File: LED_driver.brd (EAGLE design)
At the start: 53.3 x 25.4 mm, 16 parts

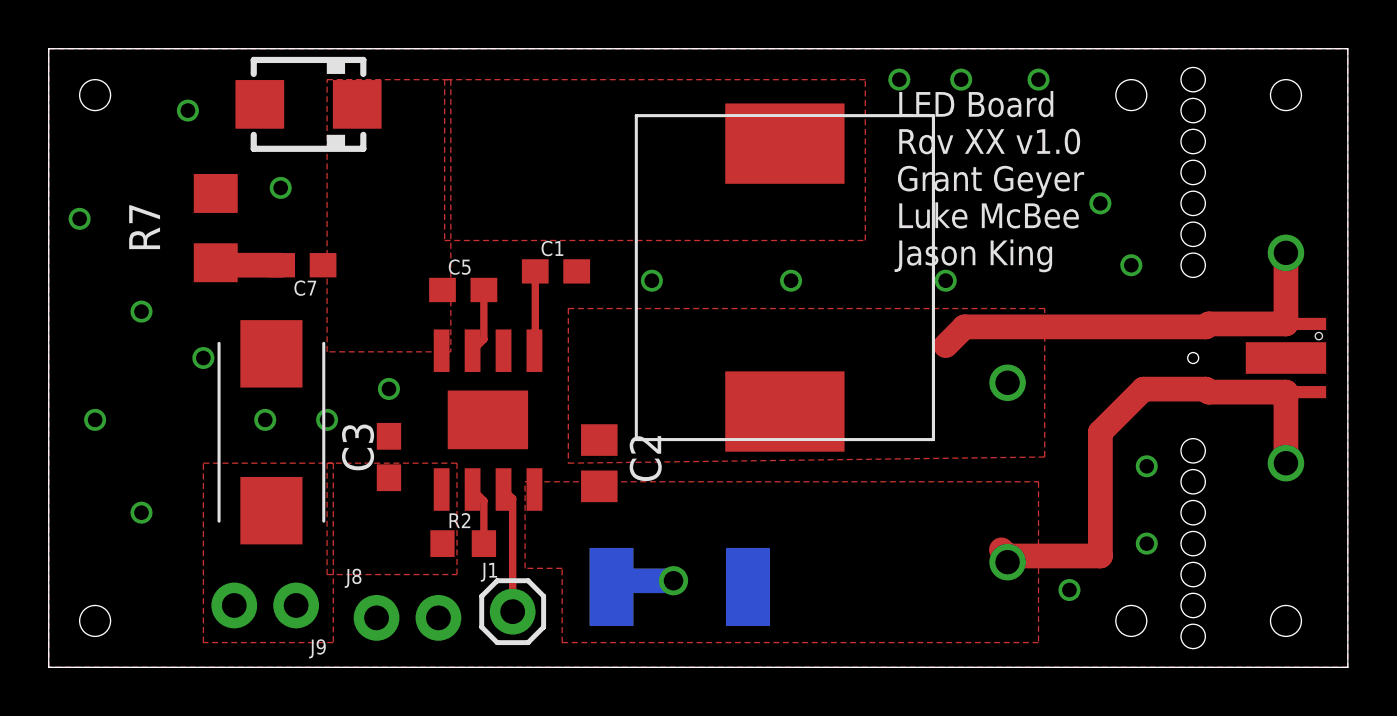
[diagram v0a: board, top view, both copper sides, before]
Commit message: added nmos and connected EN to 12V
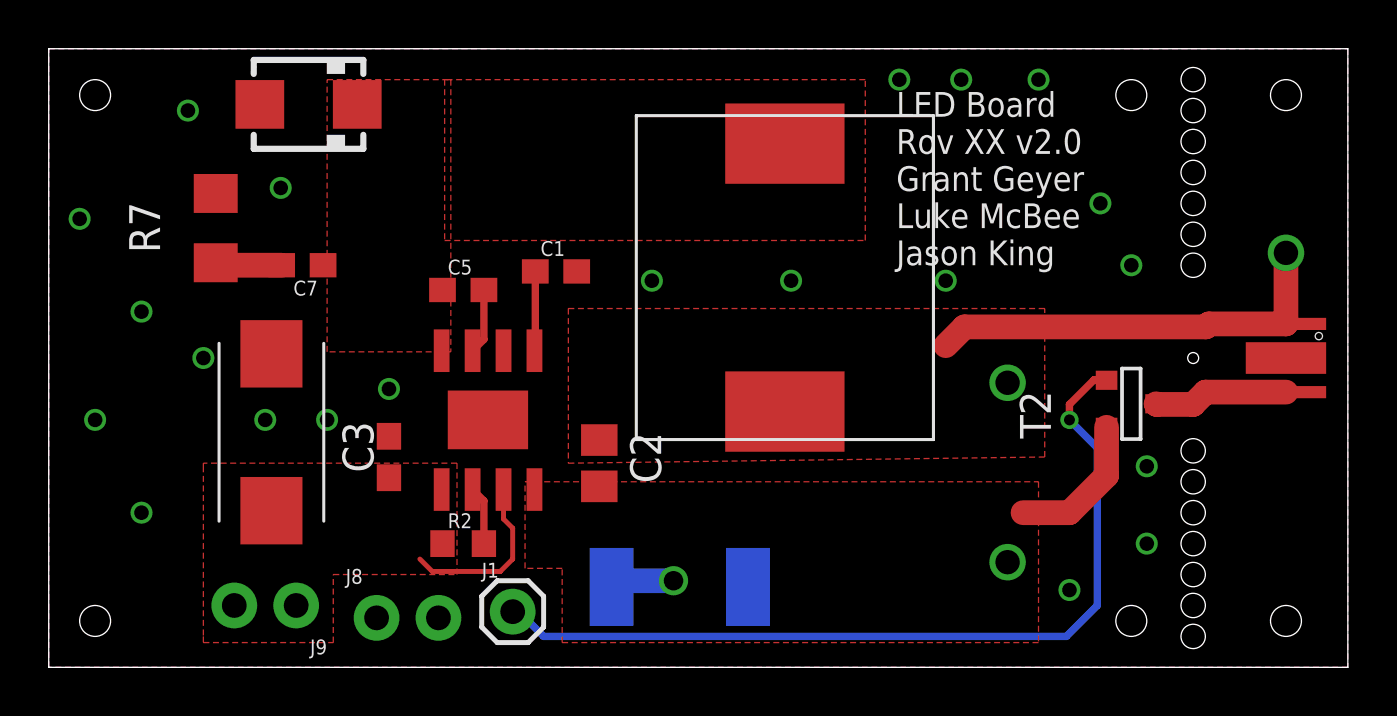
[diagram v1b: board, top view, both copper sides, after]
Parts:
- added T2: (no value), zetex:SOT-23
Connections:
- removed net LED-PWM: J1.1, U$1.3
- removed net VIN: C3.1, C8.+, J9.1, J9.2, R2.1, U$1.1
- new net 12V: C3.1, C8.+, J9.1, J9.2, R2.1, U$1.1, U$1.3
- new net LED_PWM: J1.1, T2.3
- new net N$3: T2.1, U$3.LED-
- net LED-: now also T2.2; no longer U$3.LED-
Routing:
- net LED_PWM: track 0.00 -> 35.6 mm, vias 0 -> 1
- net LED-: track 23.2 -> 8.69 mm, vias 3 -> 2
- net 12V: track 0.00 -> 7.24 mm
- net N$3: track 0.00 -> 5.55 mm
- net LED-PWM: track 5.17 -> 0.00 mm
- added copper zone on layer 1, net 12V
- removed copper zone on layer 1, net VIN
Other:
- board text added: "LED Board Rov XX v2.0 Grant Geyer Luke McBee Jason King"
- board text removed: "LED Board Rov XX v1.0 Grant Geyer Luke McBee Jason King"
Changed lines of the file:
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@@
 <?xml version="1.0" encoding="utf-8"?>
 <!DOCTYPE eagle SYSTEM "eagle.dtd">
-<eagle version="8.4.1">
+<eagle version="8.3.2">
 <drawing>
 <settings>
@@
 <setting verticaltext="up"/>
 </settings>
-<grid distance="25" unitdist="mil" unit="mil" style="lines" multiple="1" display="no" altdistance="5" altunitdist="mil" altunit="mil"/>
+<grid distance="10" unitdist="mil" unit="mil" style="lines" multiple="1" display="no" altdistance="5" altunitdist="mil" altunit="mil"/>
 <layers>
 <layer number="1" name="Top" color="4" fill="1" visible="yes" active="yes"/>
@@
 <wire x1="-5.08" y1="25.4" x2="-5.08" y2="0" width="0" layer="20"/>
 <text x="29.718" y="16.51" size="1.016" layer="21">LED Board
-Rov XX v1.0
+Rov XX v2.0
 Grant Geyer
 Luke McBee
@@
 <param name="dpMaxLengthDifference" value="10mm"/>
 <param name="dpGapFactor" value="2.5"/>
+<param name="checkGrid" value="0"/>
 <param name="checkAngle" value="0"/>
 <param name="checkFont" value="1"/>
 <param name="checkRestrict" value="0"/>
-<param name="checkStop" value="0"/>
 <param name="useDiameter" value="13"/>
 <param name="maxErrors" value="50"/>
@@
 <element name="J9" library="SparkFun-Connectors" library_urn="urn:adsk.eagle:library:513" package="1X02_NO_SILK" package3d_urn="urn:adsk.eagle:package:38051/1" value="" x="5.08" y="2.54" rot="R180"/>
 <element name="U$3" library="LED_00H53" package="LED_00H53" value="LED_00H53" x="45.72" y="12.7" rot="R270"/>
+<element name="T2" library="zetex" package="SOT-23" value="" x="39.37" y="10.795" rot="R90">
+<attribute name="MF" value="" x="31.115" y="2.54" size="1.778" layer="27" rot="R90" display="off"/>
+<attribute name="MPN" value="" x="31.115" y="2.54" size="1.778" layer="27" rot="R90" display="off"/>
+<attribute name="OC_FARNELL" value="unknown" x="31.115" y="2.54" size="1.778" layer="27" rot="R90" display="off"/>
+<attribute name="OC_NEWARK" value="unknown" x="31.115" y="2.54" size="1.778" layer="27" rot="R90" display="off"/>
+</element>
 </elements>
 <signals>
@@
 <wire x1="12.788" y1="6.836" x2="12.324" y2="7.3" width="0.3048" layer="1"/>
 </signal>
-<signal name="VIN">
+<signal name="12V">
+<contactref element="U$1" pad="3"/>
 <contactref element="U$1" pad="1"/>
 <contactref element="R2" pad="1"/>
 <contactref element="C8" pad="+"/>
 <contactref element="C3" pad="1"/>
+<wire x1="13.594" y1="7.3" x2="13.594" y2="6.091" width="0.2032" layer="1"/>
+<wire x1="13.594" y1="6.091" x2="13.97" y2="5.715" width="0.2032" layer="1"/>
+<wire x1="13.97" y1="5.715" x2="13.97" y2="4.445" width="0.2032" layer="1"/>
+<wire x1="13.97" y1="4.445" x2="13.462" y2="3.937" width="0.2032" layer="1"/>
+<wire x1="10.668" y1="3.937" x2="10.16" y2="4.445" width="0.2032" layer="1"/>
+<wire x1="13.462" y1="3.937" x2="10.668" y2="3.937" width="0.2032" layer="1"/>
 <contactref element="J9" pad="2"/>
 <contactref element="J9" pad="1"/>
-<polygon width="0.1524" layer="1">
+<polygon width="0.2032" layer="1">
+<vertex x="1.27" y="8.255"/>
+<vertex x="1.27" y="1.27"/>
 <vertex x="1.27" y="1.016"/>
-<vertex x="1.27" y="8.382"/>
-<vertex x="6.604" y="8.382"/>
 <vertex x="6.604" y="1.016"/>
-</polygon>
-<polygon width="0.1524" layer="1">
-<vertex x="6.35" y="3.81"/>
+<vertex x="6.604" y="3.81"/>
 <vertex x="11.684" y="3.81"/>
 <vertex x="11.684" y="8.382"/>
-<vertex x="6.35" y="8.382"/>
-</polygon>
-</signal>
-<signal name="LED-PWM">
-<contactref element="U$1" pad="3"/>
-<contactref element="J1" pad="1"/>
-<wire x1="13.97" y1="2.286" x2="13.97" y2="6.924" width="0.3048" layer="1"/>
-<wire x1="13.97" y1="6.924" x2="13.594" y2="7.3" width="0.3048" layer="1"/>
+<vertex x="1.27" y="8.382"/>
+</polygon>
 </signal>
 <signal name="N$4">
@@
 <contactref element="R1" pad="2"/>
 <contactref element="U$1" pad="4"/>
-<contactref element="U$3" pad="LED-"/>
 <polygon width="0.3048" layer="1">
 <vertex x="14.478" y="7.62"/>
@@
 <wire x1="20.574" y1="3.556" x2="18.282" y2="3.556" width="1.016" layer="16"/>
 <wire x1="18.282" y1="3.556" x2="18.028" y2="3.302" width="1.016" layer="16"/>
-<wire x1="42.55474375" y1="11.3" x2="45.72" y2="11.3" width="1.016" layer="1"/>
-<wire x1="42.55474375" y1="11.3" x2="42.43274375" y2="11.422" width="1.016" layer="1"/>
-<wire x1="42.43274375" y1="11.422" x2="39.87" y2="11.422" width="1.016" layer="1"/>
-<wire x1="38.1" y1="9.652" x2="38.1" y2="4.572" width="1.016" layer="1"/>
-<wire x1="38.1" y1="4.572" x2="34.29" y2="4.572" width="1.016" layer="1"/>
-<wire x1="34.29" y1="4.572" x2="34.036" y2="4.826" width="1.016" layer="1"/>
-<wire x1="39.87" y1="11.422" x2="38.1" y2="9.652" width="1.016" layer="1"/>
 <via x="34.29" y="4.318" extent="1-16" drill="1"/>
-<via x="45.72" y="8.382" extent="1-16" drill="1"/>
-<wire x1="45.72" y1="11.3" x2="45.72" y2="8.382" width="1.016" layer="1"/>
+<contactref element="T2" pad="2"/>
+<wire x1="38.354" y1="9.8552" x2="38.354" y2="7.874" width="1.016" layer="1"/>
+<wire x1="38.354" y1="7.874" x2="36.83" y2="6.35" width="1.016" layer="1"/>
+<wire x1="36.83" y1="6.35" x2="34.925" y2="6.35" width="1.016" layer="1"/>
 </signal>
 <signal name="VCC6211">
@@
 <wire x1="1.88" y1="16.51" x2="1.778" y2="16.612" width="1.016" layer="1"/>
 </signal>
+<signal name="LED_PWM">
+<contactref element="J1" pad="1"/>
+<contactref element="T2" pad="3"/>
+<wire x1="13.97" y1="2.286" x2="14.224" y2="2.286" width="0.3048" layer="16"/>
+<wire x1="14.224" y1="2.286" x2="15.24" y2="1.27" width="0.3048" layer="16"/>
+<wire x1="15.24" y1="1.27" x2="36.703" y2="1.27" width="0.3048" layer="16"/>
+<wire x1="36.703" y1="1.27" x2="37.973" y2="2.54" width="0.3048" layer="16"/>
+<wire x1="37.973" y1="9.017" x2="37.973" y2="2.54" width="0.3048" layer="16"/>
+<wire x1="37.846" y1="11.811" x2="38.3286" y2="11.811" width="0.3048" layer="1"/>
+<wire x1="38.3286" y1="11.811" x2="38.354" y2="11.7856" width="0.3048" layer="1"/>
+<wire x1="37.846" y1="11.811" x2="36.83" y2="10.795" width="0.3048" layer="1"/>
+<wire x1="36.83" y1="10.795" x2="36.83" y2="10.16" width="0.3048" layer="1"/>
+<via x="36.83" y="10.16" extent="1-16" drill="0.45"/>
+<wire x1="36.83" y1="10.16" x2="37.973" y2="9.017" width="0.3048" layer="16"/>
+</signal>
+<signal name="N$3">
+<contactref element="T2" pad="1"/>
+<contactref element="U$3" pad="LED-"/>
+<wire x1="45.72" y1="11.3" x2="42.415" y2="11.3" width="1.016" layer="1"/>
+<wire x1="42.415" y1="11.3" x2="41.91" y2="10.795" width="1.016" layer="1"/>
+<wire x1="41.91" y1="10.795" x2="40.4114" y2="10.795" width="1.016" layer="1"/>
+<wire x1="40.4114" y1="10.795" x2="40.386" y2="10.8204" width="1.016" layer="1"/>
+</signal>
 </signals>

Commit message: moved mosfet so end can still be broken off
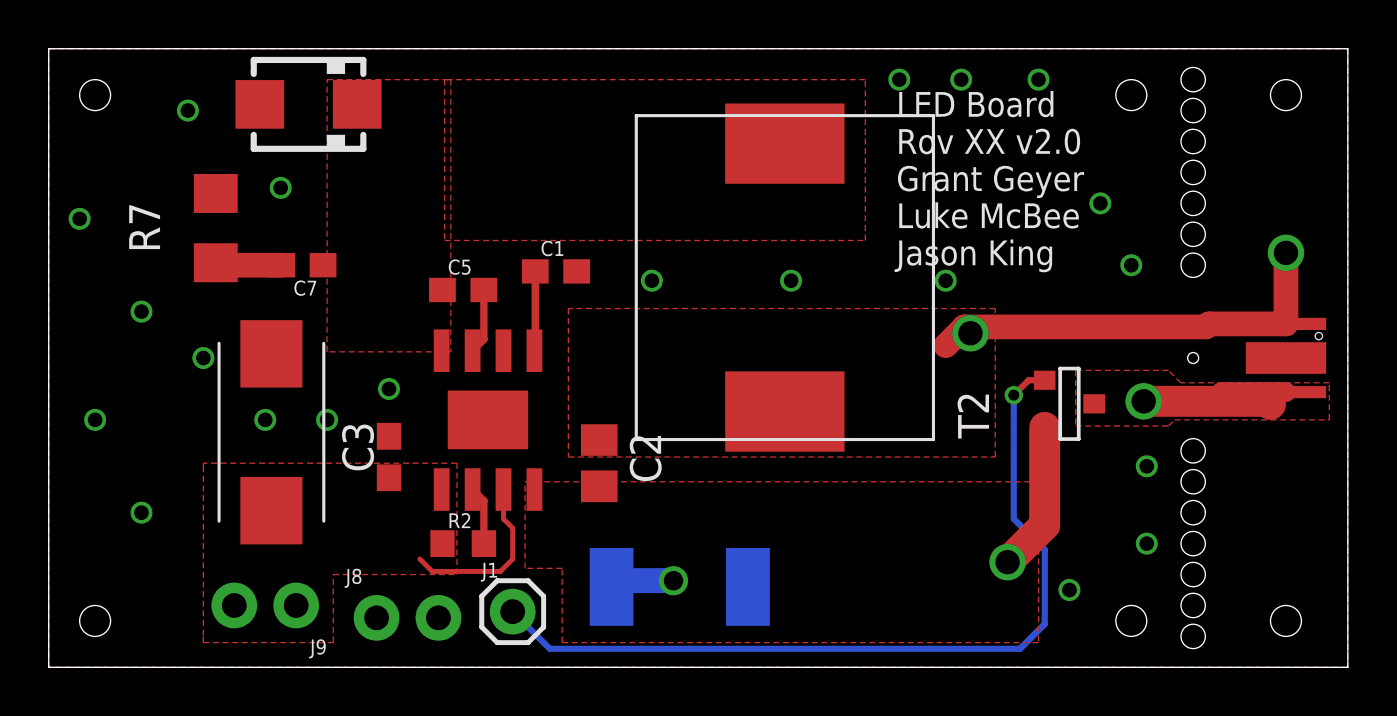
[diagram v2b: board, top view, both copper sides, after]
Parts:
- moved T2 2.54 mm to (36.8, 10.8)
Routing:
- net N$3: track 5.55 -> 7.92 mm, vias 0 -> 1
- net LED_PWM: track 35.6 -> 34.3 mm
- added copper zone on layer 1, net N$3
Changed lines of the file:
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@@
 <element name="J9" library="SparkFun-Connectors" library_urn="urn:adsk.eagle:library:513" package="1X02_NO_SILK" package3d_urn="urn:adsk.eagle:package:38051/1" value="" x="5.08" y="2.54" rot="R180"/>
 <element name="U$3" library="LED_00H53" package="LED_00H53" value="LED_00H53" x="45.72" y="12.7" rot="R270"/>
-<element name="T2" library="zetex" package="SOT-23" value="" x="39.37" y="10.795" rot="R90">
-<attribute name="MF" value="" x="31.115" y="2.54" size="1.778" layer="27" rot="R90" display="off"/>
-<attribute name="MPN" value="" x="31.115" y="2.54" size="1.778" layer="27" rot="R90" display="off"/>
-<attribute name="OC_FARNELL" value="unknown" x="31.115" y="2.54" size="1.778" layer="27" rot="R90" display="off"/>
-<attribute name="OC_NEWARK" value="unknown" x="31.115" y="2.54" size="1.778" layer="27" rot="R90" display="off"/>
+<element name="T2" library="zetex" package="SOT-23" value="" x="36.83" y="10.795" rot="R90">
+<attribute name="MF" value="" x="28.575" y="2.54" size="1.778" layer="27" rot="R90" display="off"/>
+<attribute name="MPN" value="" x="28.575" y="2.54" size="1.778" layer="27" rot="R90" display="off"/>
+<attribute name="OC_FARNELL" value="unknown" x="28.575" y="2.54" size="1.778" layer="27" rot="R90" display="off"/>
+<attribute name="OC_NEWARK" value="unknown" x="28.575" y="2.54" size="1.778" layer="27" rot="R90" display="off"/>
 </element>
 </elements>
@@
 <contactref element="U$4" pad="P$2"/>
 <contactref element="U$3" pad="LED+"/>
-<polygon width="0.3048" layer="1">
-<vertex x="16.256" y="8.382"/>
-<vertex x="35.814" y="8.636"/>
-<vertex x="35.814" y="14.732"/>
-<vertex x="16.256" y="14.732"/>
-</polygon>
 <wire x1="42.55474375" y1="14.1" x2="45.72" y2="14.1" width="1.016" layer="1"/>
 <wire x1="42.55474375" y1="14.1" x2="42.43274375" y2="13.978" width="1.016" layer="1"/>
 <wire x1="32.52" y1="13.978" x2="31.75" y2="13.208" width="1.016" layer="1"/>
 <wire x1="42.43274375" y1="13.978" x2="32.52" y2="13.978" width="1.016" layer="1"/>
-<via x="34.29" y="11.684" extent="1-16" drill="1"/>
+<via x="32.766" y="13.716" extent="1-16" drill="1"/>
 <via x="45.72" y="17.018" extent="1-16" drill="1"/>
 <wire x1="45.72" y1="14.1" x2="45.72" y2="17.018" width="1.016" layer="1"/>
+<polygon width="0.2032" layer="1">
+<vertex x="16.256" y="14.732"/>
+<vertex x="16.256" y="8.636"/>
+<vertex x="33.782" y="8.636"/>
+<vertex x="33.782" y="14.732"/>
+</polygon>
 </signal>
 <signal name="LED-">
@@
 <via x="34.29" y="4.318" extent="1-16" drill="1"/>
 <contactref element="T2" pad="2"/>
-<wire x1="38.354" y1="9.8552" x2="38.354" y2="7.874" width="1.016" layer="1"/>
-<wire x1="38.354" y1="7.874" x2="36.83" y2="6.35" width="1.016" layer="1"/>
-<wire x1="36.83" y1="6.35" x2="34.925" y2="6.35" width="1.016" layer="1"/>
+<wire x1="35.814" y1="9.8552" x2="35.814" y2="5.842" width="1.27" layer="1"/>
+<wire x1="35.814" y1="5.842" x2="34.29" y2="4.318" width="1.27" layer="1"/>
 </signal>
 <signal name="VCC6211">
@@
 <contactref element="J1" pad="1"/>
 <contactref element="T2" pad="3"/>
-<wire x1="13.97" y1="2.286" x2="14.224" y2="2.286" width="0.3048" layer="16"/>
-<wire x1="14.224" y1="2.286" x2="15.24" y2="1.27" width="0.3048" layer="16"/>
-<wire x1="15.24" y1="1.27" x2="36.703" y2="1.27" width="0.3048" layer="16"/>
-<wire x1="36.703" y1="1.27" x2="37.973" y2="2.54" width="0.3048" layer="16"/>
-<wire x1="37.973" y1="9.017" x2="37.973" y2="2.54" width="0.3048" layer="16"/>
-<wire x1="37.846" y1="11.811" x2="38.3286" y2="11.811" width="0.3048" layer="1"/>
-<wire x1="38.3286" y1="11.811" x2="38.354" y2="11.7856" width="0.3048" layer="1"/>
-<wire x1="37.846" y1="11.811" x2="36.83" y2="10.795" width="0.3048" layer="1"/>
-<wire x1="36.83" y1="10.795" x2="36.83" y2="10.16" width="0.3048" layer="1"/>
-<via x="36.83" y="10.16" extent="1-16" drill="0.45"/>
-<wire x1="36.83" y1="10.16" x2="37.973" y2="9.017" width="0.3048" layer="16"/>
+<wire x1="35.814" y1="11.7856" x2="35.1536" y2="11.7856" width="0.254" layer="1"/>
+<wire x1="35.1536" y1="11.7856" x2="34.544" y2="11.176" width="0.254" layer="1"/>
+<via x="34.544" y="11.176" extent="1-16" drill="0.45"/>
+<wire x1="34.544" y1="11.176" x2="34.544" y2="6.096" width="0.254" layer="16"/>
+<wire x1="34.544" y1="6.096" x2="35.814" y2="4.826" width="0.254" layer="16"/>
+<wire x1="35.814" y1="4.826" x2="35.814" y2="1.778" width="0.254" layer="16"/>
+<wire x1="35.814" y1="1.778" x2="34.798" y2="0.762" width="0.254" layer="16"/>
+<wire x1="34.798" y1="0.762" x2="15.494" y2="0.762" width="0.254" layer="16"/>
+<wire x1="15.494" y1="0.762" x2="13.97" y2="2.286" width="0.254" layer="16"/>
 </signal>
 <signal name="N$3">
 <contactref element="T2" pad="1"/>
 <contactref element="U$3" pad="LED-"/>
-<wire x1="45.72" y1="11.3" x2="42.415" y2="11.3" width="1.016" layer="1"/>
-<wire x1="42.415" y1="11.3" x2="41.91" y2="10.795" width="1.016" layer="1"/>
-<wire x1="41.91" y1="10.795" x2="40.4114" y2="10.795" width="1.016" layer="1"/>
-<wire x1="40.4114" y1="10.795" x2="40.386" y2="10.8204" width="1.016" layer="1"/>
+<polygon width="0.2032" layer="1" isolate="0.254">
+<vertex x="37.084" y="12.192"/>
+<vertex x="37.084" y="9.906"/>
+<vertex x="40.894" y="9.906"/>
+<vertex x="41.148" y="10.16"/>
+<vertex x="47.498" y="10.16"/>
+<vertex x="47.498" y="11.684"/>
+<vertex x="41.402" y="11.684"/>
+<vertex x="40.894" y="12.192"/>
+</polygon>
+<wire x1="45.72" y1="11.3" x2="43.056" y2="11.3" width="0.8128" layer="1"/>
+<wire x1="43.056" y1="11.3" x2="42.926" y2="11.43" width="0" layer="19" extent="1-16"/>
+<via x="39.878" y="10.922" extent="1-16" drill="1"/>
+<wire x1="39.878" y1="10.922" x2="44.958" y2="10.922" width="1.27" layer="1"/>
+<wire x1="44.958" y1="10.922" x2="45.085" y2="10.795" width="1.27" layer="1"/>
 </signal>
 </signals>
